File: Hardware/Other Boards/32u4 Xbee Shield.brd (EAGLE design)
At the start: 27.9 x 41.9 mm, 20 parts, among them Q1 MOSFET-NCHANNELSMD, Q2 MOSFET-NCHANNELSMD, U2 XBEE-1B3, U3 V_REG_LDOSMD

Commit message: 32u4 Xbee Shield
32u4 Xbee Shield
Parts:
- moved Q1 5.12 mm to (16.5, 24.1)
- moved Q2 5.12 mm to (11.4, 24.1)
- moved R6 5.12 mm to (17.8, 29.8)
- moved R8 5.12 mm to (12.7, 29.8)
- moved R5 5.12 mm to (15.2, 29.8)
- moved R7 5.12 mm to (10.2, 29.8)
- moved U2 0.64 mm to (14.0, 41.9)
- moved R11 0.64 mm to (14.0, 21.0)
- moved U$1 0.64 mm to (14.0, 21.0)
- moved LED1 0.63 mm to (14.0, 9.53)
- moved LED2 0.63 mm to (12.1, 12.1)
- moved LED3 0.63 mm to (14.0, 12.1)
- moved LED4 0.63 mm to (15.9, 12.1)
- moved C1 0.63 mm to (17.8, 36.2)
- moved C2 0.63 mm to (14.0, 40.0)
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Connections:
- net 5V: now also U$1.P$3
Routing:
- net 3.3V: track 0.00 -> 69.3 mm
- net 5V: track 0.00 -> 59.4 mm, vias 0 -> 1
- net OUT: track 0.00 -> 34.3 mm, vias 0 -> 2
- net IN: track 0.00 -> 30.5 mm, vias 0 -> 4
- net RSSI: track 0.00 -> 21.5 mm, vias 0 -> 2
- net N$38: track 0.00 -> 11.7 mm
- net DIN: track 0.00 -> 7.39 mm
- net DOUT: track 0.00 -> 5.94 mm

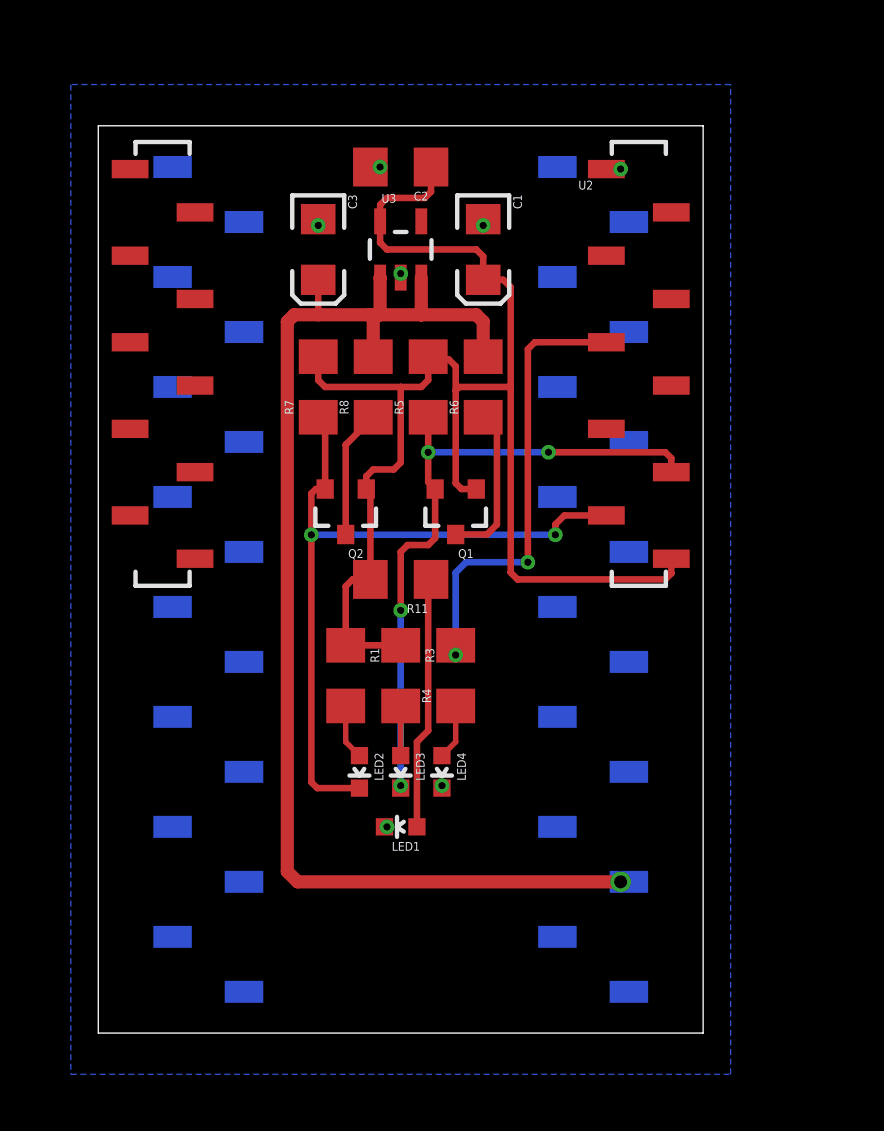
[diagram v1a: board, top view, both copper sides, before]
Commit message: Moved things around on xbee shield
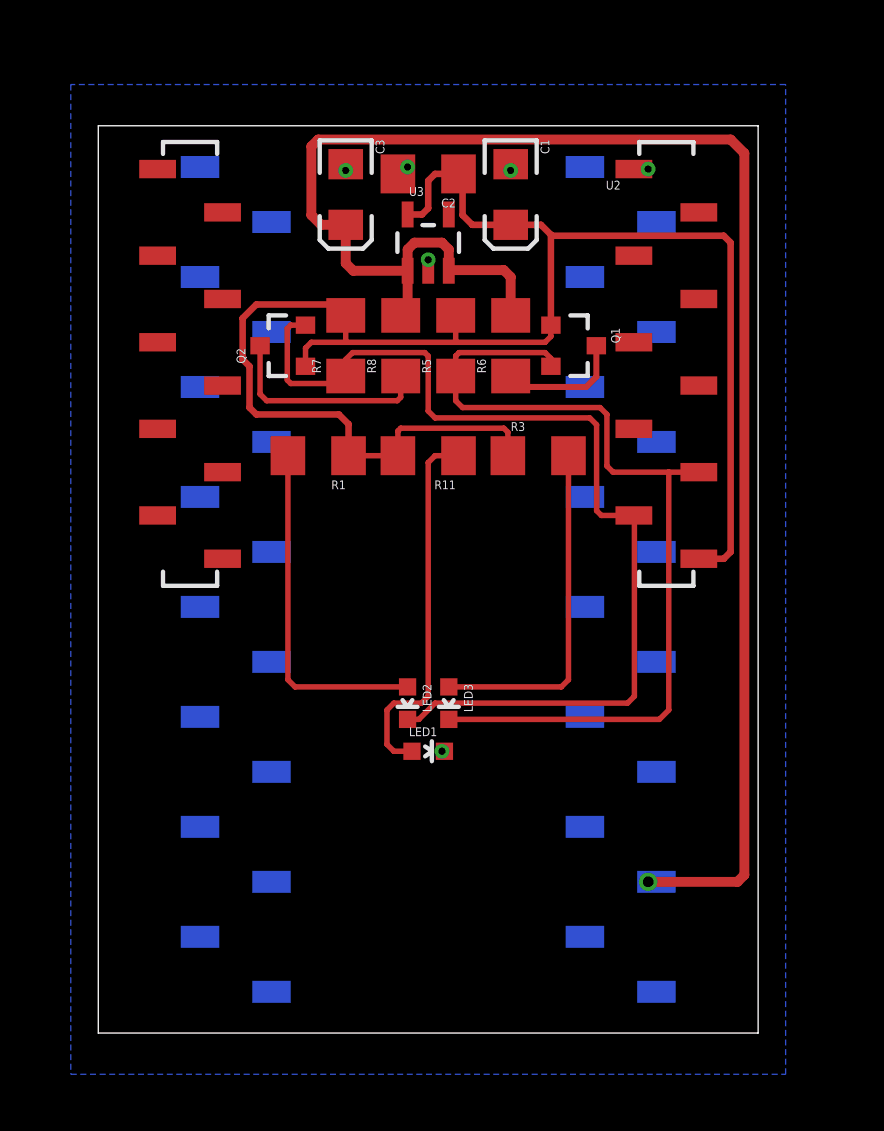
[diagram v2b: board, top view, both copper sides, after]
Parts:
- removed LED4: Green, SparkFun:LED-0603
- removed R4: 1k, SparkFun-Passives:1206
- moved R3 12.0 mm to (20.3, 26.7), turned to 0 degrees
- moved R1 10.2 mm to (10.2, 26.7), turned to 180 degrees
- moved Q1 9.34 mm to (21.9, 31.8), turned to 270 degrees
- moved Q2 8.14 mm to (8.57, 31.8), turned to 90 degrees
- moved R11 5.85 mm to (15.2, 26.7)
- moved LED2 3.88 mm to (14.3, 15.2)
- moved LED3 3.88 mm to (16.2, 15.2)
- moved LED1 3.72 mm to (15.2, 13.0), turned to 270 degrees
- moved C1 2.84 mm to (19.1, 38.7)
- moved C3 2.84 mm to (11.4, 38.7)
- moved R5 2.29 mm to (16.5, 31.8)
- moved R8 2.29 mm to (14.0, 31.8)
- moved R6 2.29 mm to (19.1, 31.8)
- moved R7 2.29 mm to (11.4, 31.8)
- moved C2 1.31 mm to (15.2, 39.7)
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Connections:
- removed net N$2: LED4.A, R4.1
- net GND: no longer LED4.C
- net RSSI: no longer R4.2
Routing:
- net RSSI: track 21.5 -> 0.00 mm, vias 2 -> 0
- net 5V: track 59.4 -> 79.7 mm
- net N$4: track 2.29 -> 16.0 mm
- net N$1: track 2.56 -> 16.0 mm
- net OUT: track 34.3 -> 46.7 mm, vias 2 -> 0
- net IN: track 30.5 -> 42.3 mm, vias 4 -> 0
- net 3.3V: track 69.3 -> 80.2 mm
- net N$38: track 11.7 -> 17.4 mm
- net DOUT: track 5.94 -> 9.91 mm
- net N$2: track 2.56 -> 0.00 mm
- net DIN: track 7.39 -> 5.80 mm
- net GND: track 2.10 -> 2.41 mm, vias 7 -> 6
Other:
- board size 27.9 x 41.9 mm -> 30.5 x 41.9 mm

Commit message: Power on the xbee shield
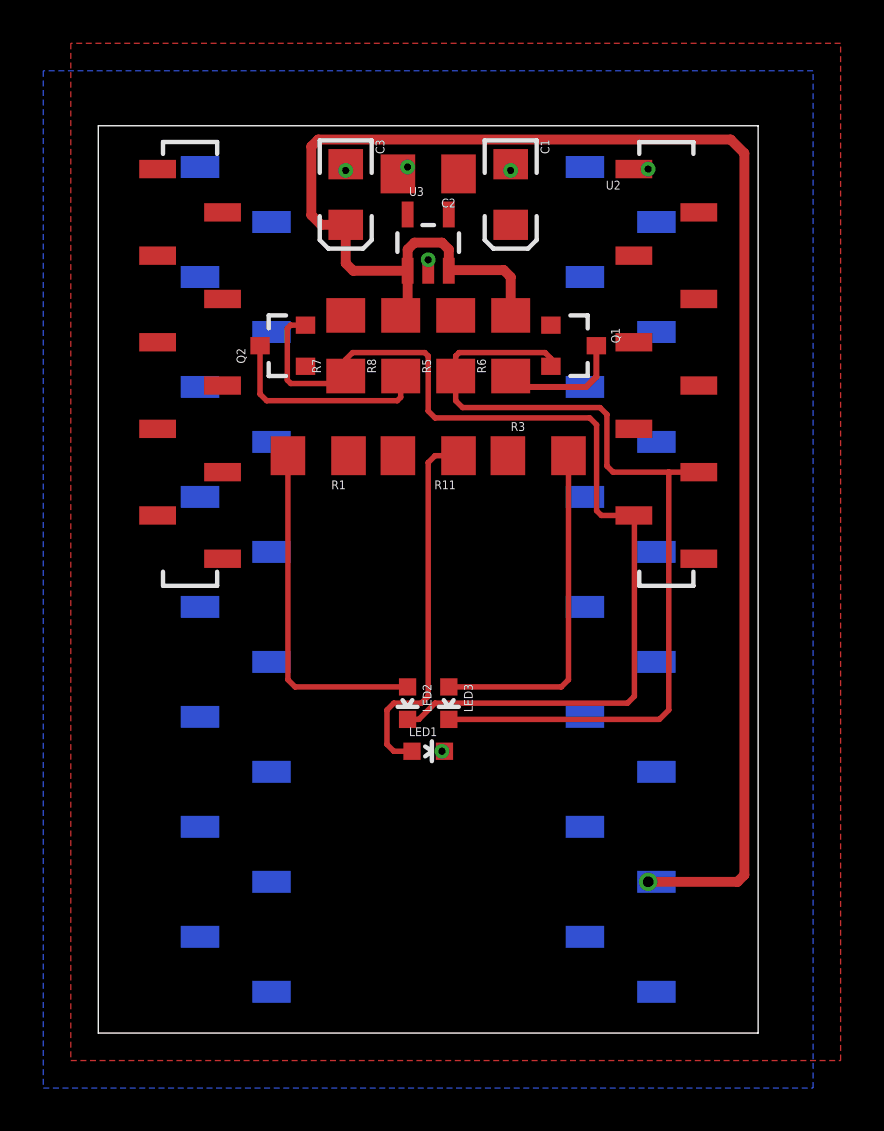
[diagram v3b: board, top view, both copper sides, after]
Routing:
- net 3.3V: track 80.2 -> 0.00 mm
- added copper zone on layer 1, net 3.3V
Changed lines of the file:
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@@
 <?xml version="1.0" encoding="utf-8"?>
 <!DOCTYPE eagle SYSTEM "eagle.dtd">
-<eagle version="7.1.0">
+<eagle version="6.5.0">
 <drawing>
 <settings>
@@
 <pass name="Default">
 <param name="RoutingGrid" value="50mil"/>
-<param name="AutoGrid" value="1"/>
-<param name="Efforts" value="0"/>
-<param name="TopRouterVariant" value="1"/>
 <param name="tpViaShape" value="round"/>
-<param name="PrefDir.1" value="a"/>
+<param name="PrefDir.1" value="|"/>
 <param name="PrefDir.2" value="0"/>
 <param name="PrefDir.3" value="0"/>
@@
 <param name="PrefDir.14" value="0"/>
 <param name="PrefDir.15" value="0"/>
-<param name="PrefDir.16" value="a"/>
+<param name="PrefDir.16" value="-"/>
 <param name="cfVia" value="8"/>
 <param name="cfNonPref" value="5"/>
@@
 <signals>
 <signal name="GND">
-<polygon width="0.4064" layer="16">
-<vertex x="-1.27" y="43.815"/>
-<vertex x="-1.27" y="-1.905"/>
-<vertex x="31.75" y="-1.905"/>
-<vertex x="31.75" y="43.815"/>
+<polygon width="0.3048" layer="16">
+<vertex x="-2.54" y="44.45"/>
+<vertex x="-2.54" y="-2.54"/>
+<vertex x="33.02" y="-2.54"/>
+<vertex x="33.02" y="44.45"/>
 </polygon>
 <contactref element="U$1" pad="P$2"/>
@@
 <contactref element="R7" pad="2"/>
 <contactref element="Q2" pad="1"/>
-<wire x1="14.29" y1="37.8126" x2="14.9526" y2="37.8126" width="0.3048" layer="1"/>
-<wire x1="14.9526" y1="37.8126" x2="15.24" y2="38.1" width="0.3048" layer="1"/>
-<wire x1="15.24" y1="38.1" x2="15.24" y2="39.37" width="0.3048" layer="1"/>
-<wire x1="15.24" y1="39.37" x2="15.5575" y2="39.6875" width="0.3048" layer="1"/>
-<wire x1="15.5575" y1="39.6875" x2="16.64" y2="39.6875" width="0.3048" layer="1"/>
-<wire x1="19.05" y1="37.335" x2="17.275" y2="37.335" width="0.3048" layer="1"/>
-<wire x1="17.275" y1="37.335" x2="16.8275" y2="37.7825" width="0.3048" layer="1"/>
-<wire x1="16.8275" y1="37.7825" x2="16.8275" y2="39.8175" width="0.3048" layer="1"/>
-<wire x1="16.8275" y1="39.8175" x2="16.64" y2="39.6875" width="0.3048" layer="1"/>
-<wire x1="19.05" y1="37.335" x2="20.45" y2="37.335" width="0.3048" layer="1"/>
-<wire x1="20.9075" y1="32.7" x2="20.9075" y2="36.8775" width="0.3048" layer="1"/>
-<wire x1="20.9075" y1="36.8775" x2="20.45" y2="37.335" width="0.3048" layer="1"/>
-<wire x1="9.5725" y1="30.8" x2="9.5725" y2="31.63875" width="0.254" layer="1"/>
-<wire x1="9.5725" y1="31.63875" x2="9.8425" y2="31.90875" width="0.254" layer="1"/>
-<wire x1="9.8425" y1="31.90875" x2="11.43" y2="31.90875" width="0.254" layer="1"/>
-<wire x1="11.43" y1="31.90875" x2="16.51" y2="31.90875" width="0.254" layer="1"/>
-<wire x1="16.51" y1="31.90875" x2="20.6375" y2="31.90875" width="0.254" layer="1"/>
-<wire x1="20.6375" y1="31.90875" x2="20.9075" y2="32.17875" width="0.254" layer="1"/>
-<wire x1="20.9075" y1="32.7" x2="20.9075" y2="32.17875" width="0.254" layer="1"/>
-<wire x1="16.51" y1="33.15" x2="16.51" y2="31.90875" width="0.254" layer="1"/>
-<wire x1="11.43" y1="33.15" x2="11.43" y2="31.90875" width="0.254" layer="1"/>
-<wire x1="11.56" y1="26.67" x2="13.84" y2="26.67" width="0.254" layer="1"/>
-<wire x1="18.92" y1="26.67" x2="18.92" y2="27.7525" width="0.254" layer="1"/>
-<wire x1="18.92" y1="27.7525" x2="18.7325" y2="27.94" width="0.254" layer="1"/>
-<wire x1="18.7325" y1="27.94" x2="13.97" y2="27.94" width="0.254" layer="1"/>
-<wire x1="13.84" y1="26.67" x2="13.84" y2="27.81" width="0.254" layer="1"/>
-<wire x1="13.84" y1="27.81" x2="13.97" y2="27.94" width="0.254" layer="1"/>
-<wire x1="11.56" y1="26.67" x2="11.56" y2="28.1275" width="0.3048" layer="1"/>
-<wire x1="11.56" y1="28.1275" x2="11.1125" y2="28.575" width="0.3048" layer="1"/>
-<wire x1="11.1125" y1="28.575" x2="7.3025" y2="28.575" width="0.3048" layer="1"/>
-<wire x1="7.3025" y1="28.575" x2="6.985" y2="28.8925" width="0.3048" layer="1"/>
-<wire x1="6.985" y1="28.8925" x2="6.985" y2="30.7975" width="0.3048" layer="1"/>
-<wire x1="6.985" y1="30.7975" x2="6.6675" y2="31.115" width="0.3048" layer="1"/>
-<wire x1="6.6675" y1="31.115" x2="6.6675" y2="33.02" width="0.3048" layer="1"/>
-<wire x1="6.6675" y1="33.02" x2="7.3025" y2="33.655" width="0.3048" layer="1"/>
-<wire x1="7.3025" y1="33.655" x2="11.2425" y2="33.655" width="0.3048" layer="1"/>
-<wire x1="11.2425" y1="33.655" x2="11.43" y2="33.15" width="0.3048" layer="1"/>
-<wire x1="27.74" y1="21.91" x2="28.895" y2="21.91" width="0.3048" layer="1"/>
-<wire x1="28.895" y1="21.91" x2="29.21" y2="22.225" width="0.3048" layer="1"/>
-<wire x1="29.21" y1="22.225" x2="29.21" y2="36.5125" width="0.3048" layer="1"/>
-<wire x1="29.21" y1="36.5125" x2="28.8925" y2="36.83" width="0.3048" layer="1"/>
-<wire x1="28.8925" y1="36.83" x2="20.955" y2="36.83" width="0.3048" layer="1"/>
-<wire x1="20.955" y1="36.83" x2="20.9075" y2="36.8775" width="0.3048" layer="1"/>
+<polygon width="0.3048" layer="1">
+<vertex x="-1.27" y="45.72"/>
+<vertex x="-1.27" y="-1.27"/>
+<vertex x="34.29" y="-1.27"/>
+<vertex x="34.29" y="45.72"/>
+</polygon>
 </signal>
 <signal name="DIO4">
